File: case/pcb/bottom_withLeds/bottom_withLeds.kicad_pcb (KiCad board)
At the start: 2 copper layers, 141.5 x 115.5 mm, 9 parts

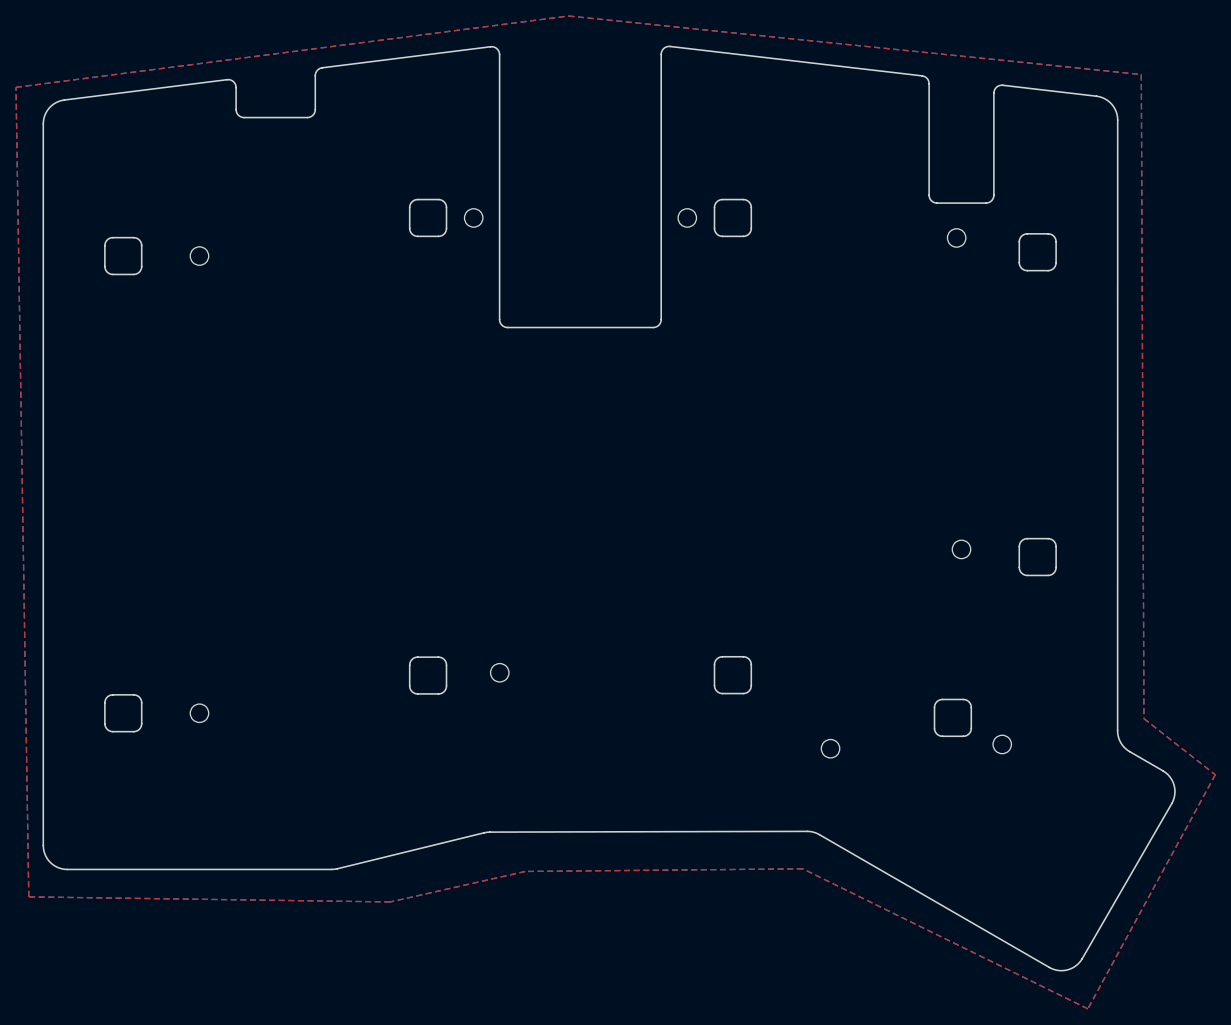
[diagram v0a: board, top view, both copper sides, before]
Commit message: add bottom pcb cases different types
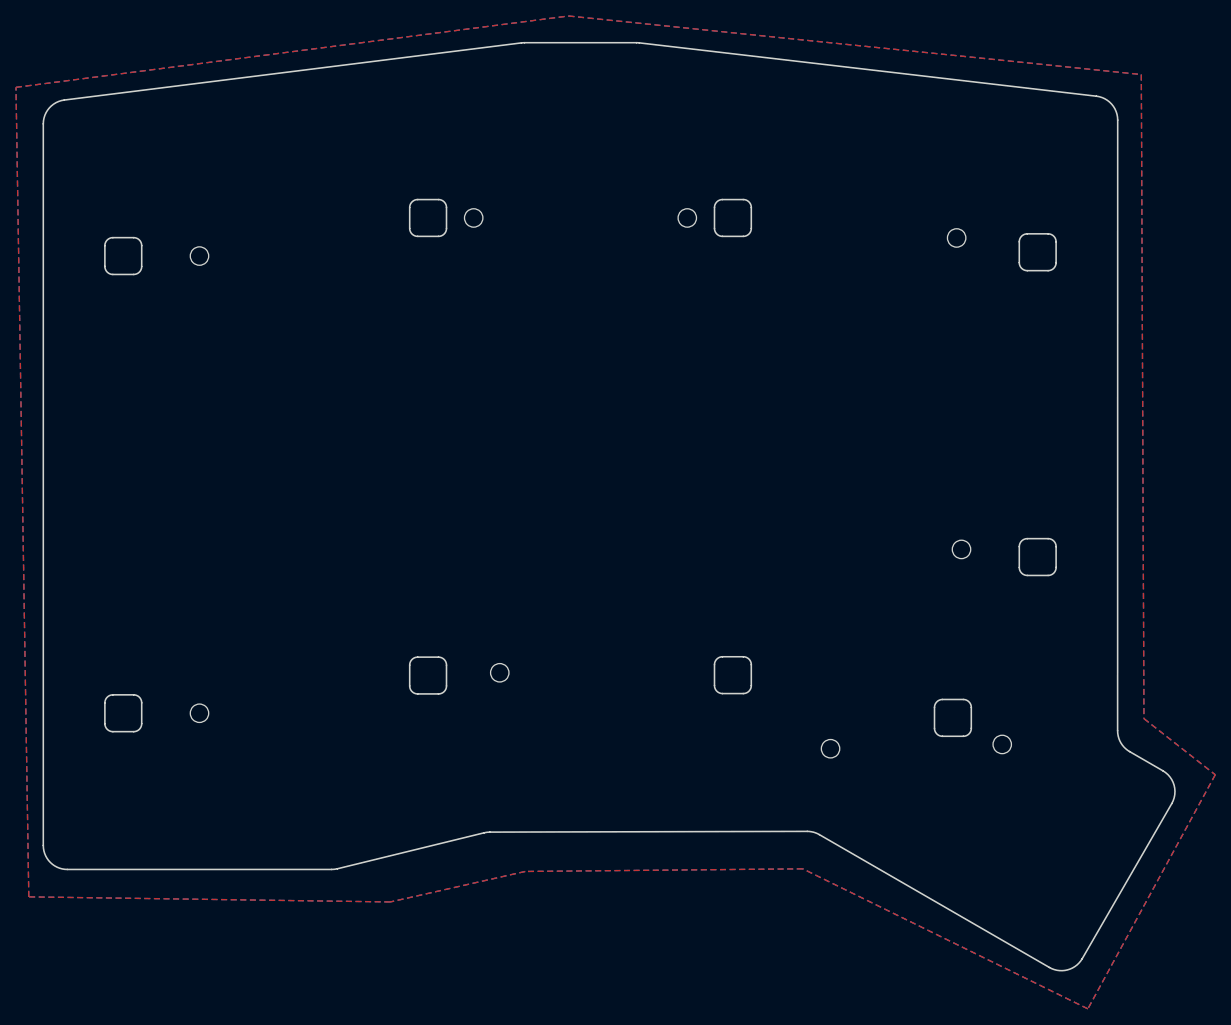
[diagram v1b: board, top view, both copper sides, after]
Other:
- board size 141.5 x 115.5 mm -> 141.5 x 116 mm
